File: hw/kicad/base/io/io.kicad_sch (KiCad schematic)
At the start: 9 parts, among them J1 SPI, J2 PWM1, J3 UART 1, J4 I2C, J5 PWM2, J6 UART 2, J7 ADC, J8 TOP, J9 BUTTOM

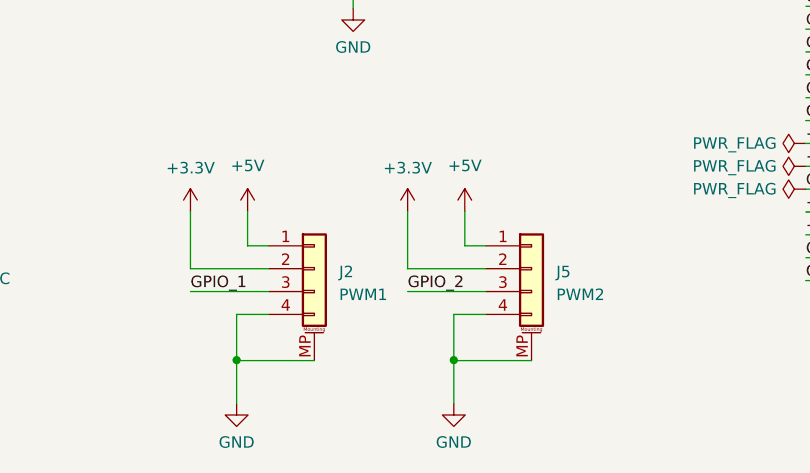
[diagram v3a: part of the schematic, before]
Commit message: 更新power16v一些错误
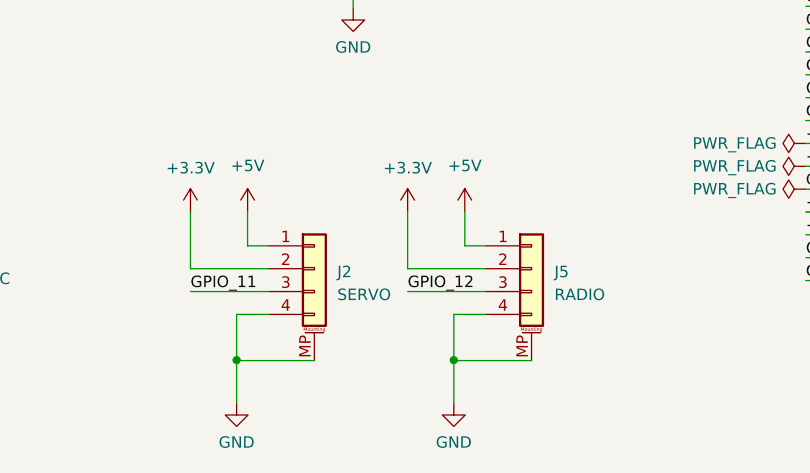
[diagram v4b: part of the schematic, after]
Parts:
- J2: value PWM1 -> SERVO
- J5: value PWM2 -> RADIO
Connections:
- net GPIO_1: no longer J2.3 (Pin_3)
- net GPIO_11: now also J2.3 (Pin_3)
- net GPIO_12: now also J5.3 (Pin_3)
- net GPIO_2: no longer J5.3 (Pin_3)
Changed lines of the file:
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@@
     (effects (font (size 1.27 1.27)) (justify right bottom))
   )
-  (label "GPIO_1" (at 125.9332 110.4392 0) (fields_autoplaced)
+  (label "GPIO_11" (at 125.9332 110.4392 0) (fields_autoplaced)
     (effects (font (size 1.27 1.27)) (justify left bottom))
   )
@@
     (effects (font (size 1.27 1.27)) (justify left bottom))
   )
-  (label "GPIO_2" (at 150.0632 110.4392 0) (fields_autoplaced)
+  (label "GPIO_12" (at 150.0632 110.4392 0) (fields_autoplaced)
     (effects (font (size 1.27 1.27)) (justify left bottom))
   )
@@
   (symbol (lib_id "Connector_Generic_MountingPin:Conn_01x04_MountingPin") (at 163.83 107.8992 0) (unit 1)
     (in_bom yes) (on_board yes) (dnp no) (fields_autoplaced)
-    (property "Reference" "J5" (at 166.5732 108.2548 0)
+    (property "Reference" "J5" (at 166.37 108.2548 0)
       (effects (font (size 1.27 1.27)) (justify left))
     )
-    (property "Value" "PWM2" (at 166.5732 110.7948 0)
+    (property "Value" "RADIO" (at 166.37 110.7948 0)
       (effects (font (size 1.27 1.27)) (justify left))
     )
@@
   (symbol (lib_id "Connector_Generic_MountingPin:Conn_01x04_MountingPin") (at 139.7 107.8992 0) (unit 1)
     (in_bom yes) (on_board yes) (dnp no) (fields_autoplaced)
-    (property "Reference" "J2" (at 142.4432 108.2548 0)
+    (property "Reference" "J2" (at 142.24 108.2548 0)
       (effects (font (size 1.27 1.27)) (justify left))
     )
-    (property "Value" "PWM1" (at 142.4432 110.7948 0)
+    (property "Value" "SERVO" (at 142.24 110.7948 0)
       (effects (font (size 1.27 1.27)) (justify left))
     )
